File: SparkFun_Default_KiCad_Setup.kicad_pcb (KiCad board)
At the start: 4 copper layers, 50.8 x 50.8 mm, 12 parts

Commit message: Add silkscreen color to ordering instructions
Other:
- board text added: "Silkscreen Color: White"
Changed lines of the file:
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@@
     (effects (font (size 1.5 1.5) (thickness 0.3) bold) (justify bottom))
   )
-  (gr_text "No Clean Process" (at 166.320892 123.13059) (layer "F.Fab")
+  (gr_text "No Clean Process" (at 166.320892 125.73) (layer "F.Fab")
     (effects (font (size 2 2) (thickness 0.15)) (justify left bottom))
   )
-  (gr_text "Inner Copper Weight: 0.5oz" (at 166.37 131.1275) (layer "F.Fab")
+  (gr_text "Inner Copper Weight: 0.5oz" (at 166.37 133.72691) (layer "F.Fab")
     (effects (font (size 2 2) (thickness 0.15)) (justify left bottom))
   )
-  (gr_text "Layers: 4" (at 166.320892 112.97059) (layer "F.Fab")
+  (gr_text "Layers: 4" (at 166.320892 115.57) (layer "F.Fab")
+    (effects (font (size 2 2) (thickness 0.15)) (justify left bottom))
+  )
+  (gr_text "Silkscreen Color: White" (at 166.37 113.03) (layer "F.Fab")
     (effects (font (size 2 2) (thickness 0.15)) (justify left bottom))
   )
@@
     (effects (font (size 2 2) (thickness 0.15)) (justify left bottom))
   )
-  (gr_text "Material: TG155" (at 166.320892 125.67059) (layer "F.Fab")
+  (gr_text "Material: TG155" (at 166.320892 128.27) (layer "F.Fab")
     (effects (font (size 2 2) (thickness 0.15)) (justify left bottom))
   )
-  (gr_text "Controlled Impedance: JLC7628" (at 166.2958 115.495) (layer "F.Fab")
+  (gr_text "Controlled Impedance: JLC7628" (at 166.2958 118.09441) (layer "F.Fab")
     (effects (font (size 2 2) (thickness 0.15)) (justify left bottom))
   )
-  (gr_text "Outer Copper Weight: 1oz" (at 166.37 128.27) (layer "F.Fab")
+  (gr_text "Outer Copper Weight: 1oz" (at 166.37 130.86941) (layer "F.Fab")
     (effects (font (size 2 2) (thickness 0.15)) (justify left bottom))
   )
-  (gr_text "Thickness: 1.6mm" (at 166.320892 120.59059) (layer "F.Fab")
+  (gr_text "Thickness: 1.6mm" (at 166.320892 123.19) (layer "F.Fab")
     (effects (font (size 2 2) (thickness 0.15)) (justify left bottom))
   )
-  (gr_text "Finish: ENIG" (at 166.320892 118.05059) (layer "F.Fab")
+  (gr_text "Finish: ENIG" (at 166.320892 120.65) (layer "F.Fab")
     (effects (font (size 2 2) (thickness 0.15)) (justify left bottom))
   )

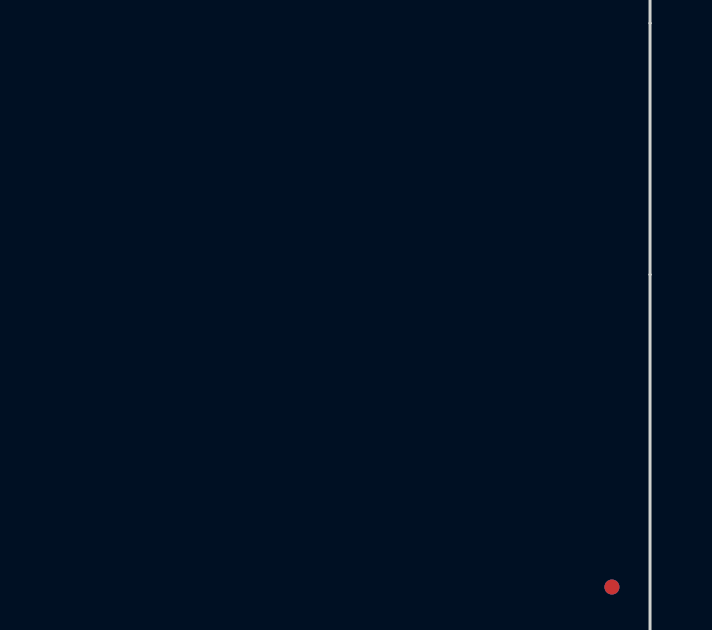
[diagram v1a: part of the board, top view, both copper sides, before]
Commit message: Remove islands from polygon.
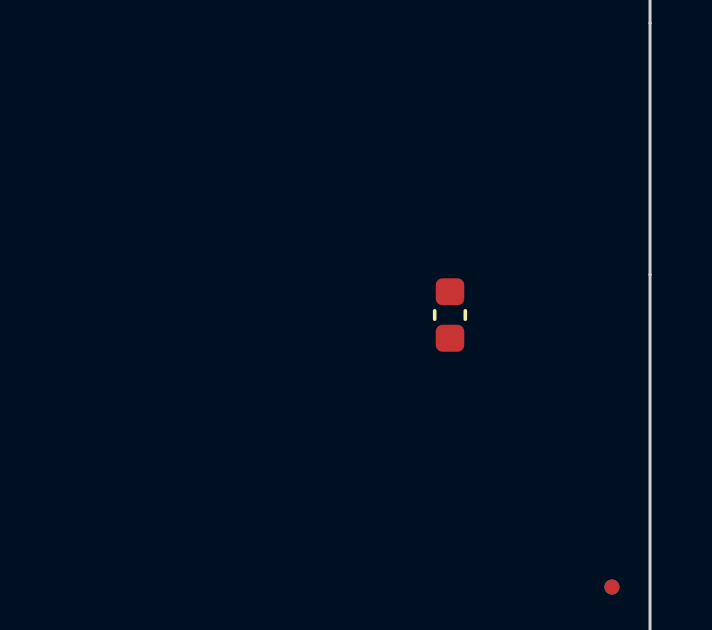
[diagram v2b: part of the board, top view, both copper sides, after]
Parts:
- added C1: 0.1uF, SparkFun-Capacitor:C_0603_1608Metric, F.Cu at (145.7, 137.0)
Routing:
- added copper zone on B.Cu, net GND
- added copper zone on F.Cu, net GND
- added copper zone on In1.Cu, net GND
- removed copper zone on B.Cu, net (none)
- removed copper zone on F.Cu, net (none)
- removed copper zone on In1.Cu, net (none)
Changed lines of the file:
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@@
   )
   (net 0 "")
+  (net 1 "3.3V")
+  (net 2 "GND")
   (footprint "SparkFun-Hardware:STAND-OFF" (layer "F.Cu")
     (at 149.86 149.86)
@@
     (pad "" np_thru_hole circle (at 0 0) (size 3.302 3.302) (drill 3.302) (layers "F&B.Cu" "*.Mask"))
   )
+  (footprint "SparkFun-Capacitor:C_0603_1608Metric" (layer "F.Cu")
+    (at 145.7325 136.9825 90)
+    (tags "capacitor")
+    (property "PROD_ID" "CAP-00810")
+    (property "Sheetfile" "SparkFun_Default_KiCad_Setup.kicad_sch")
+    (property "Sheetname" "")
+    (property "Tolerance" "+80%/-20%")
+    (property "Voltage" "25V")
+    (property "ki_description" "Unpolarized capacitor")
+    (property "ki_keywords" "cap capacitor")
+    (attr smd)
+    (fp_text reference "C1" (at 0 -1.43 90) (layer "F.Fab")
+        (effects (font (size 0.5 0.5) (thickness 0.1) bold))
+    )
+    (fp_text value "0.1uF" (at 0 1.43 90) (layer "F.Fab")
+        (effects (font (size 0.5 0.5) (thickness 0.1) bold))
+    )
+    (fp_line (start -0.14058 -0.51) (end 0.14058 -0.51)
+      (stroke (width 0.12) (type solid)) (layer "F.SilkS"))
+    (fp_line (start -0.14058 0.51) (end 0.14058 0.51)
+      (stroke (width 0.12) (type solid)) (layer "F.SilkS"))
+    (fp_line (start -1.48 -0.73) (end 1.48 -0.73)
+      (stroke (width 0.05) (type solid)) (layer "F.CrtYd"))
+    (fp_line (start -1.48 0.73) (end -1.48 -0.73)
+      (stroke (width 0.05) (type solid)) (layer "F.CrtYd"))
+    (fp_line (start 1.48 -0.73) (end 1.48 0.73)
+      (stroke (width 0.05) (type solid)) (layer "F.CrtYd"))
+    (fp_line (start 1.48 0.73) (end -1.48 0.73)
+      (stroke (width 0.05) (type solid)) (layer "F.CrtYd"))
+    (fp_line (start -0.8 -0.4) (end 0.8 -0.4)
+      (stroke (width 0.1) (type solid)) (layer "F.Fab"))
+    (fp_line (start -0.8 0.4) (end -0.8 -0.4)
+      (stroke (width 0.1) (type solid)) (layer "F.Fab"))
+    (fp_line (start 0.8 -0.4) (end 0.8 0.4)
+      (stroke (width 0.1) (type solid)) (layer "F.Fab"))
+    (fp_line (start 0.8 0.4) (end -0.8 0.4)
+      (stroke (width 0.1) (type solid)) (layer "F.Fab"))
+    (pad "1" smd roundrect (at -0.775 0 90) (size 0.9 0.95) (layers "F.Cu" "F.Paste" "F.Mask") (roundrect_rratio 0.25)
+      (net 1 "3.3V") (pintype "passive"))
+    (pad "2" smd roundrect (at 0.775 0 90) (size 0.9 0.95) (layers "F.Cu" "F.Paste" "F.Mask") (roundrect_rratio 0.25)
+      (net 2 "GND") (pintype "passive"))
+    (model "${KICAD6_3DMODEL_DIR}/Capacitor_SMD.3dshapes/C_0603_1608Metric.wrl"
+      (offset (xyz 0 0 0))
+      (scale (xyz 1 1 1))
+      (rotate (xyz 0 0 0))
+    )
+  )
   (footprint "SparkFun-Aesthetic:Creative_Commons_License" (layer "F.Cu")
     (at 107.95 163.83)
@@
     (style (thickness 0.15) (arrow_length 1.27) (text_position_mode 0) (extension_height 0.58642) (extension_offset 0.5) keep_text_aligned)
   )
-  (zone (net 0) (net_name "") (layers "F.Cu" "In1.Cu" "B.Cu") (hatch edge 0.5)
+  (zone (net 2) (net_name "GND") (layers "F.Cu" "In1.Cu" "B.Cu") (hatch edge 0.5)
     (connect_pads (clearance 0.1778))
     (min_thickness 0.1778) (filled_areas_thickness no)
-    (fill yes (thermal_gap 0.1778) (thermal_bridge_width 0.1778) (island_removal_mode 1) (island_area_min 9.999999))
+    (fill yes (thermal_gap 0.1778) (thermal_bridge_width 0.1778))
     (polygon
       (pts

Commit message: Update parts to new naming scheme
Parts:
- ST1, ST2, ST3, ST4: footprint SparkFun-Hardware:STAND-OFF -> SparkFun-Hardware:Standoff
- U1: footprint SparkFun-Aesthetic:ORDERING_INSTRUCTIONS -> SparkFun-Aesthetic:Ordering_Instructions
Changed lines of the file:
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@@
   (net 1 "3.3V")
   (net 2 "GND")
-  (footprint "SparkFun-Hardware:STAND-OFF" (layer "F.Cu")
+  (footprint "SparkFun-Hardware:Standoff" (layer "F.Cu")
     (at 149.86 149.86)
     (property "Sheetfile" "SparkFun_Default_KiCad_Setup.kicad_sch")
@@
     (pad "" np_thru_hole circle (at 0 0) (size 3.302 3.302) (drill 3.302) (layers "F&B.Cu" "*.Mask"))
   )
-  (footprint "SparkFun-Aesthetic:ORDERING_INSTRUCTIONS" (layer "F.Cu")
+  (footprint "SparkFun-Aesthetic:Ordering_Instructions" (layer "F.Cu")
     (at 165.1 101.6)
     (property "Sheetfile" "SparkFun_Default_KiCad_Setup.kicad_sch")
@@
       (solder_mask_margin 0.25) (clearance 0.25))
   )
-  (footprint "SparkFun-Hardware:STAND-OFF" (layer "F.Cu")
+  (footprint "SparkFun-Hardware:Standoff" (layer "F.Cu")
     (at 149.86 104.14)
     (property "Sheetfile" "SparkFun_Default_KiCad_Setup.kicad_sch")
@@
     )
   )
-  (footprint "SparkFun-Hardware:STAND-OFF" (layer "F.Cu")
+  (footprint "SparkFun-Hardware:Standoff" (layer "F.Cu")
     (at 104.14 104.14)
     (property "Sheetfile" "SparkFun_Default_KiCad_Setup.kicad_sch")
@@
     )
   )
-  (footprint "SparkFun-Hardware:STAND-OFF" (layer "F.Cu")
+  (footprint "SparkFun-Hardware:Standoff" (layer "F.Cu")
     (at 104.14 149.86)
     (property "Sheetfile" "SparkFun_Default_KiCad_Setup.kicad_sch")

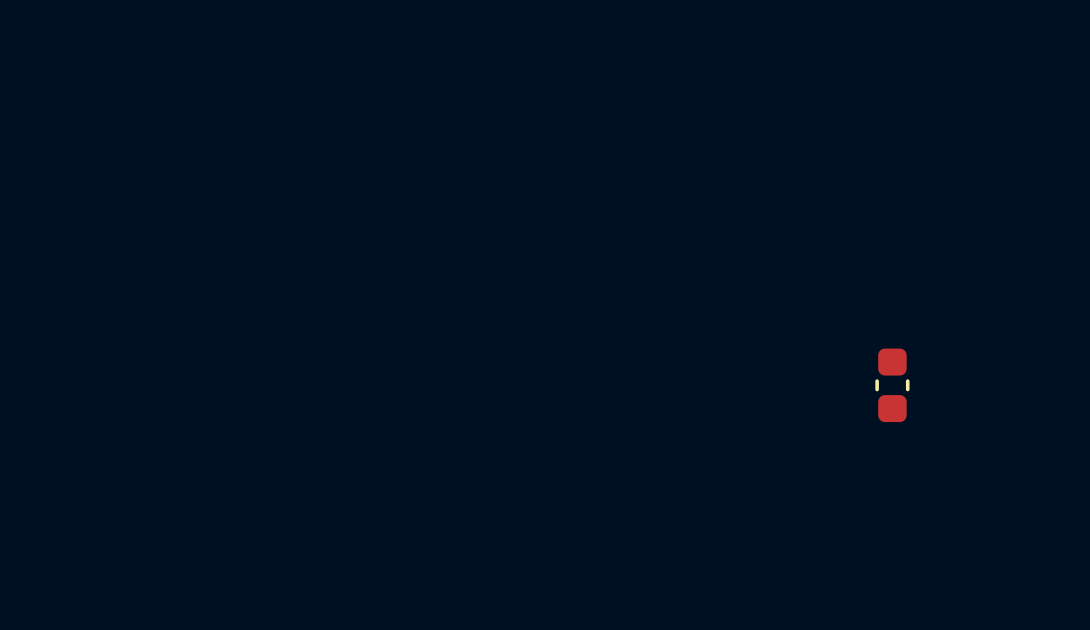
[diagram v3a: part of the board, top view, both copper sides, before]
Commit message: Add basic regulator circuit to show various components
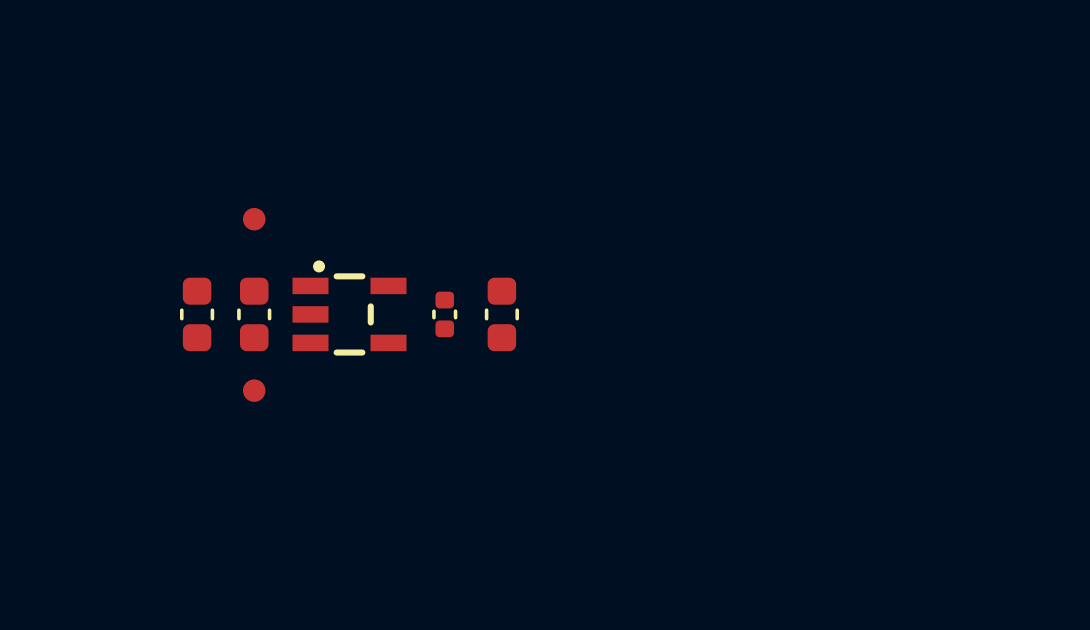
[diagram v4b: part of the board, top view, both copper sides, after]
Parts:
- removed C1: 0.1uF, SparkFun-Capacitor:C_0603_1608Metric
- added C2: 10uF, SparkFun-Capacitor:C_0603_1608Metric, F.Cu at (122.6, 134.6)
- added C3: 1.0uF, SparkFun-Capacitor:C_0603_1608Metric, F.Cu at (124.5, 134.6)
- added C4: 1.0uF, SparkFun-Capacitor:C_0402_1005Metric, F.Cu at (130.8, 134.6)
- added C5: 10uF, SparkFun-Capacitor:C_0603_1608Metric, F.Cu at (132.7, 134.6)
- added TP1: TestPoint_0.75mm, SparkFun-Connector:TestPoint-0.75mm, F.Cu at (124.5, 137.2)
- added TP2: TestPoint_0.75mm, SparkFun-Connector:TestPoint-0.75mm, F.Cu at (124.5, 131.4)
- added U2: RT9080-3.3, SparkFun-Semiconductor-Standard:SOT23-5, F.Cu at (127.6, 134.6)

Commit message: Removing ordering instruction from SCH. Adding notes to PCB.
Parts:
- removed U1: ~, SparkFun-Aesthetic:Ordering_Instructions
- moved G3 123.8 mm to (231.8, 163.2)
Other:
- board text added: "Ordering Notes"
- board text removed: "You"
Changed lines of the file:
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@@
   )
   (paper "A4")
+  (title_block
+    (comment 1 "Designed by: You")
+  )
   (layers
     (0 "F.Cu" signal)
@@
   (net 3 "VCC")
   (net 4 "unconnected-(U2-NC-Pad4)")
+  (footprint "SparkFun-Aesthetic:Creative_Commons_License" (layer "F.Cu")
+    (at 231.775 163.195)
+    (tags "Creative Commons License")
+    (property "Sheetfile" "SparkFun_Default_KiCad_Setup.kicad_sch")
+    (property "Sheetname" "")
+    (property "exclude_from_bom" "")
+    (property "ki_keywords" "Open Source Hardware Logo")
+    (attr exclude_from_bom)
+    (fp_text reference "G3" (at 0 -5.08) (layer "F.Fab") hide
+        (effects (font (size 1.27 1.27) (thickness 0.15)))
+    )
+    (fp_text value "OSHW_Logo" (at 0 2.794) (layer "F.Fab") hide
+        (effects (font (size 1.27 1.27) (thickness 0.15)))
+    )
+    (fp_text user "Released under the Creative Commons Attribution Share-Alike 4.0 License" (at 0 -1.27) (layer "User.1")
+        (effects (font (size 1.63576 1.63576) (thickness 0.14224)) (justify bottom))
+    )
+    (fp_text user " https://creativecommons.org/licenses/by-sa/4.0/" (at 0 1.27) (layer "User.1")
+        (effects (font (size 1.63576 1.63576) (thickness 0.14224)) (justify bottom))
+    )
+  )
   (footprint "SparkFun-Semiconductor-Standard:SOT23-5" (layer "F.Cu")
     (at 127.635 134.62)
@@
     (pad "" np_thru_hole circle (at 0 0) (size 3.302 3.302) (drill 3.302) (layers "F&B.Cu" "*.Mask"))
   )
-  (footprint "SparkFun-Aesthetic:Ordering_Instructions" (layer "F.Cu")
-    (at 165.1 101.6)
-    (property "Sheetfile" "SparkFun_Default_KiCad_Setup.kicad_sch")
-    (property "Sheetname" "")
-    (fp_text reference "U1" (at 2.54 -1.27) (layer "F.Fab") hide
-        (effects (font (size 1.27 1.27) (thickness 0.15)))
-    )
-    (fp_text value "~" (at 2.54 -2.54) (layer "F.Fab") hide
-        (effects (font (size 1.27 1.27) (thickness 0.15)))
-    )
-    (fp_text user "Ordering Instructions:" (at 1.27 1.27) (layer "User.1")
-        (effects (font (size 2.5908 2.5908) (thickness 0.4572)) (justify left top))
-    )
-    (fp_line (start 0 4.445) (end 63.5 4.445)
-      (stroke (width 0.2032) (type solid)) (layer "User.1"))
-    (fp_rect (start 0 0) (end 63.5 50.8)
-      (stroke (width 0.2) (type default)) (fill none) (layer "User.1"))
-  )
   (footprint "SparkFun-Aesthetic:Fiducial_0.5mm_Mask1mm" (layer "F.Cu")
     (at 151.13 146.05)
@@
     (pad "" np_thru_hole circle (at 0 0) (size 3.302 3.302) (drill 3.302) (layers "F&B.Cu" "*.Mask"))
   )
-  (footprint "SparkFun-Aesthetic:Creative_Commons_License" (layer "F.Cu")
-    (at 107.95 163.83)
-    (tags "Creative Commons License")
-    (property "Sheetfile" "SparkFun_Default_KiCad_Setup.kicad_sch")
-    (property "Sheetname" "")
-    (property "exclude_from_bom" "")
-    (property "ki_keywords" "Open Source Hardware Logo")
-    (attr exclude_from_bom)
-    (fp_text reference "G3" (at 0 -5.08) (layer "F.Fab") hide
-        (effects (font (size 1.27 1.27) (thickness 0.15)))
-    )
-    (fp_text value "OSHW_Logo" (at 0 6.35) (layer "F.Fab") hide
-        (effects (font (size 1.27 1.27) (thickness 0.15)))
-    )
-    (fp_text user "Designed by:" (at 0 3.81) (layer "Cmts.User")
-        (effects (font (size 1.63576 1.63576) (thickness 0.14224)) (justify bottom))
-    )
-    (fp_text user "Released under the Creative Commons Attribution Share-Alike 4.0 License" (at 0 -1.27) (layer "Cmts.User")
-        (effects (font (size 1.63576 1.63576) (thickness 0.14224)) (justify bottom))
-    )
-    (fp_text user " https://creativecommons.org/licenses/by-sa/4.0/" (at 0 1.27) (layer "Cmts.User")
-        (effects (font (size 1.63576 1.63576) (thickness 0.14224)) (justify bottom))
-    )
-  )
   (footprint "SparkFun-Capacitor:C_0402_1005Metric" (layer "F.Cu")
     (at 130.81 134.62 -90)
@@
     (effects (font (size 1.016 1.016) (thickness 0.254) bold) (justify mirror))
   )
-  (gr_text "You" (at 121.92 167.64) (layer "Cmts.User")
-    (effects (font (size 1.5 1.5) (thickness 0.3) bold) (justify bottom))
+  (gr_text "No Clean Process" (at 241.935 176.53) (layer "F.Fab")
+    (effects (font (size 1.27 1.27) (thickness 0.15)) (justify left bottom))
   )
-  (gr_text "No Clean Process" (at 166.320892 125.73) (layer "F.Fab")
-    (effects (font (size 2 2) (thickness 0.15)) (justify left bottom))
+  (gr_text "Inner Copper Weight: 0.5oz" (at 241.935 180.34) (layer "F.Fab")
+    (effects (font (size 1.27 1.27) (thickness 0.15)) (justify left bottom))
   )
-  (gr_text "Inner Copper Weight: 0.5oz" (at 166.37 133.72691) (layer "F.Fab")
-    (effects (font (size 2 2) (thickness 0.15)) (justify left bottom))
+  (gr_text "Layers: 4" (at 211.405892 176.53) (layer "F.Fab")
+    (effects (font (size 1.27 1.27) (thickness 0.15)) (justify left bottom))
   )
-  (gr_text "Layers: 4" (at 166.320892 115.57) (layer "F.Fab")
-    (effects (font (size 2 2) (thickness 0.15)) (justify left bottom))
+  (gr_text "Silkscreen Color: White" (at 211.455 174.625) (layer "F.Fab")
+    (effects (font (size 1.27 1.27) (thickness 0.15)) (justify left bottom))
   )
-  (gr_text "Silkscreen Color: White" (at 166.37 113.03) (layer "F.Fab")
-    (effects (font (size 2 2) (thickness 0.15)) (justify left bottom))
+  (gr_text "Solder Mask: Red" (at 211.455 172.72) (layer "F.Fab")
+    (effects (font (size 1.27 1.27) (thickness 0.15)) (justify left bottom))
   )
-  (gr_text "Solder Mask: Red" (at 166.320892 110.43059) (layer "F.Fab")
-    (effects (font (size 2 2) (thickness 0.15)) (justify left bottom))
+  (gr_text "Material: TG155" (at 241.935 174.625) (layer "F.Fab")
+    (effects (font (size 1.27 1.27) (thickness 0.15)) (justify left bottom))
   )
-  (gr_text "Material: TG155" (at 166.320892 128.27) (layer "F.Fab")
-    (effects (font (size 2 2) (thickness 0.15)) (justify left bottom))
+  (gr_text "Controlled Impedance: JLC7628" (at 241.935 172.72) (layer "F.Fab")
+    (effects (font (size 1.27 1.27) (thickness 0.15)) (justify left bottom))
   )
-  (gr_text "Controlled Impedance: JLC7628" (at 166.2958 118.09441) (layer "F.Fab")
-    (effects (font (size 2 2) (thickness 0.15)) (justify left bottom))
+  (gr_text "Outer Copper Weight: 1oz" (at 241.935 178.435) (layer "F.Fab")
+    (effects (font (size 1.27 1.27) (thickness 0.15)) (justify left bottom))
   )
-  (gr_text "Outer Copper Weight: 1oz" (at 166.37 130.86941) (layer "F.Fab")
-    (effects (font (size 2 2) (thickness 0.15)) (justify left bottom))
+  (gr_text "Thickness: 1.6mm" (at 211.455 178.435) (layer "F.Fab")
+    (effects (font (size 1.27 1.27) (thickness 0.15)) (justify left bottom))
   )
-  (gr_text "Thickness: 1.6mm" (at 166.320892 123.19) (layer "F.Fab")
-    (effects (font (size 2 2) (thickness 0.15)) (justify left bottom))
+  (gr_text "Finish: ENIG" (at 211.455 180.34) (layer "F.Fab")
+    (effects (font (size 1.27 1.27) (thickness 0.15)) (justify left bottom))
   )
-  (gr_text "Finish: ENIG" (at 166.320892 120.65) (layer "F.Fab")
+  (gr_text "Ordering Notes" (at 205.105 169.545) (layer "F.Fab")
     (effects (font (size 2 2) (thickness 0.15)) (justify left bottom))
   )
@@
     (pts (xy 101.6 101.6) (xy 152.4 101.6))
     (height -3.81)
-    (gr_text "2000 mils" (at 127 96.64) (layer "Dwgs.User")
+    (gr_text "50.8 mm" (at 127 96.64) (layer "Dwgs.User")
       (effects (font (size 1 1) (thickness 0.15)))
     )
@@
     (pts (xy 152.4 152.4) (xy 152.4 149.86))
     (height 2.54)
-    (gr_text "100 mils" (at 153.79 151.13 90) (layer "Dwgs.User")
+    (gr_text "2.5 mm" (at 153.79 151.13 90) (layer "Dwgs.User")
       (effects (font (size 1 1) (thickness 0.15)))
     )
@@
     (pts (xy 101.6 152.4) (xy 104.14 152.4))
     (height 2.54)
-    (gr_text "100 mils" (at 102.87 153.79) (layer "Dwgs.User")
+    (gr_text "2.5 mm" (at 102.87 153.79) (layer "Dwgs.User")
       (effects (font (size 1 1) (thickness 0.15)))
     )
@@
     (pts (xy 101.6 152.4) (xy 101.6 101.6))
     (height -3.81)
-    (gr_text "2000 mils" (at 96.64 127 90) (layer "Dwgs.User")
+    (gr_text "50.8 mm" (at 96.64 127 90) (layer "Dwgs.User")
       (effects (font (size 1 1) (thickness 0.15)))
     )
